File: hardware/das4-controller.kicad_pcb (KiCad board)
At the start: 2 copper layers, 51.1 x 94 mm, 16 parts, among them J1 USB-C (upstream, USB 2.0), J2 USB-A (hub port 1), J3 USB-A (hub port 2), J4 Key matrix 26p (TBD: pitch/ty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, SW1 Button, SW2 Button, SW3 Button, SW4 Button, SW5 Button

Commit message: Move volume encoder to its real position
The first photo trace located the top of the ~20 mm shaft, which
parallax shifted ~3 mm outward. Measured on the fit-check print against
the 50 mm scale bar, the body sits about flush with the bottom edge:
shaft centre (10.0, 5.8) instead of (10.6, 2.5).

Co-Authored-By: Claude Opus 5.5 <noreply@anthropic.com>
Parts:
- moved ENC1 3.35 mm to (112.5, 136.7)

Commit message: Use a no-switch encoder; knob has 20 detents and doesn't push
The original knob doesn't press, and a push-switch encoder can't fit:
with the body flush against the board edge its switch pins would land
off the board. Swap to the no-switch footprint, drop the encoder push
from the GPIO budget (36 pins) and record 20 detents per turn.

Co-Authored-By: Claude Opus 5.5 <noreply@anthropic.com>
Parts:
- ENC1: value Volume encoder (PEC12R-42xxF-S0024?) -> Volume encoder, no switch, 20 detents; footprint RotaryEncoder_Alps_EC12E-Switch_Vertical_H20mm -> RotaryEncoder_Alps_EC12E_Vertical_H20mm

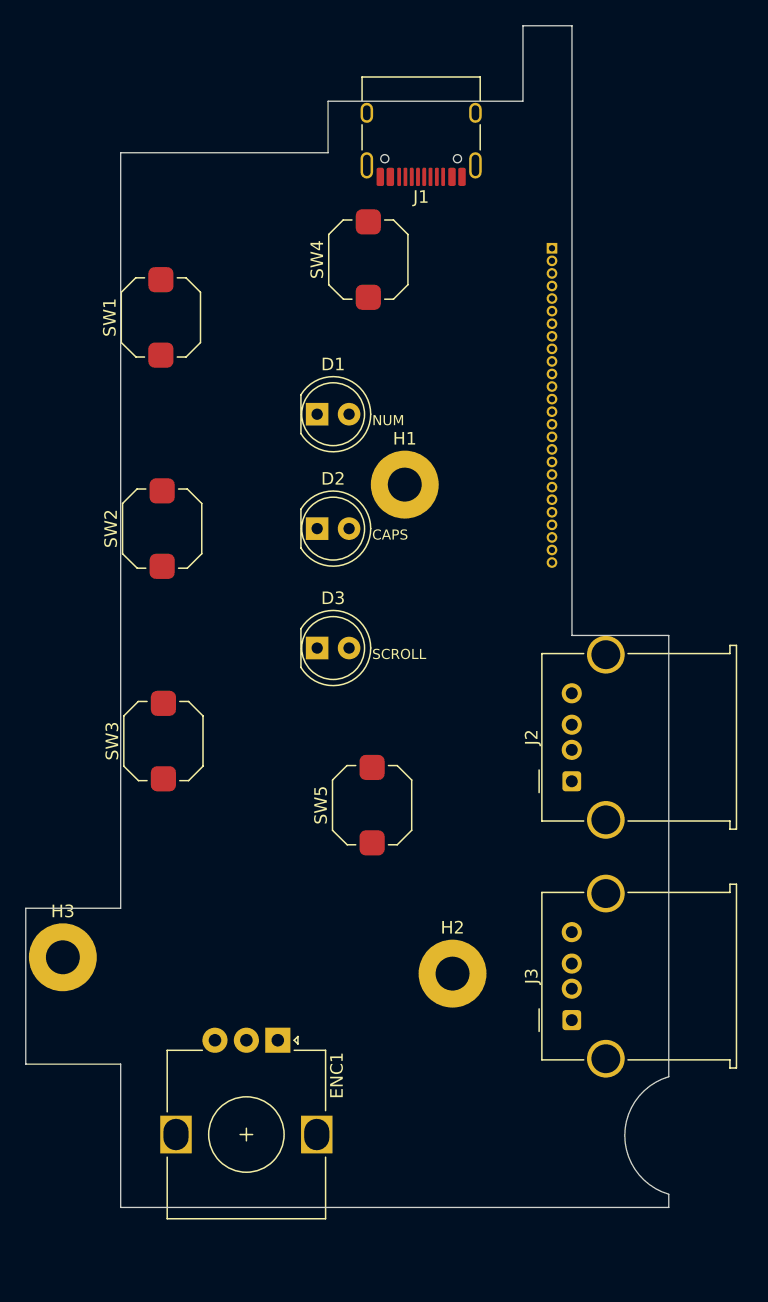
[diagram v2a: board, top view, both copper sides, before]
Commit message: Circuit in SKiDL, JLCPCB parts, and a placed 4-layer board
The circuit is now code (hardware/circuit/das4.py) and every part is a
real, in-stock JLCPCB part:
- RP2350B core copied from Raspberry Pi's minimal design (crystal, QSPI
  flash, 1.1 V regulator inductor, decoupling, BOOTSEL/RESET, SWD pads)
- CH334R USB 2.0 hub: USB-C upstream, two USB-A ports and the MCU
  downstream, powered from 3.3 V per the WCH datasheet; ESD on every
  port, polyfuses on the USB-A VBUS lines
- ME6211 3.3 V LDO, Alps EC12E no-switch encoder, 5 buttons, three
  5 V-driven lock LEDs, 26 key-matrix lines to GPIO21-46

The board is generated from the netlist: measured mechanical parts stay
put, everything else is placed in groups, on 4 layers with JLCPCB rules.
DRC is clean apart from routing, cosmetic silkscreen, and the CAPS LED
next to H1 (same as the original board).

Footprints, symbols and 3D models come from LCSC via easyeda2kicad, so
pads match what JLCPCB solders. docs/bom.md lists parts with live stock
(74 parts, ~$9 per board, 14 Extended types).

Co-Authored-By: Claude Opus 5.5 <noreply@anthropic.com>
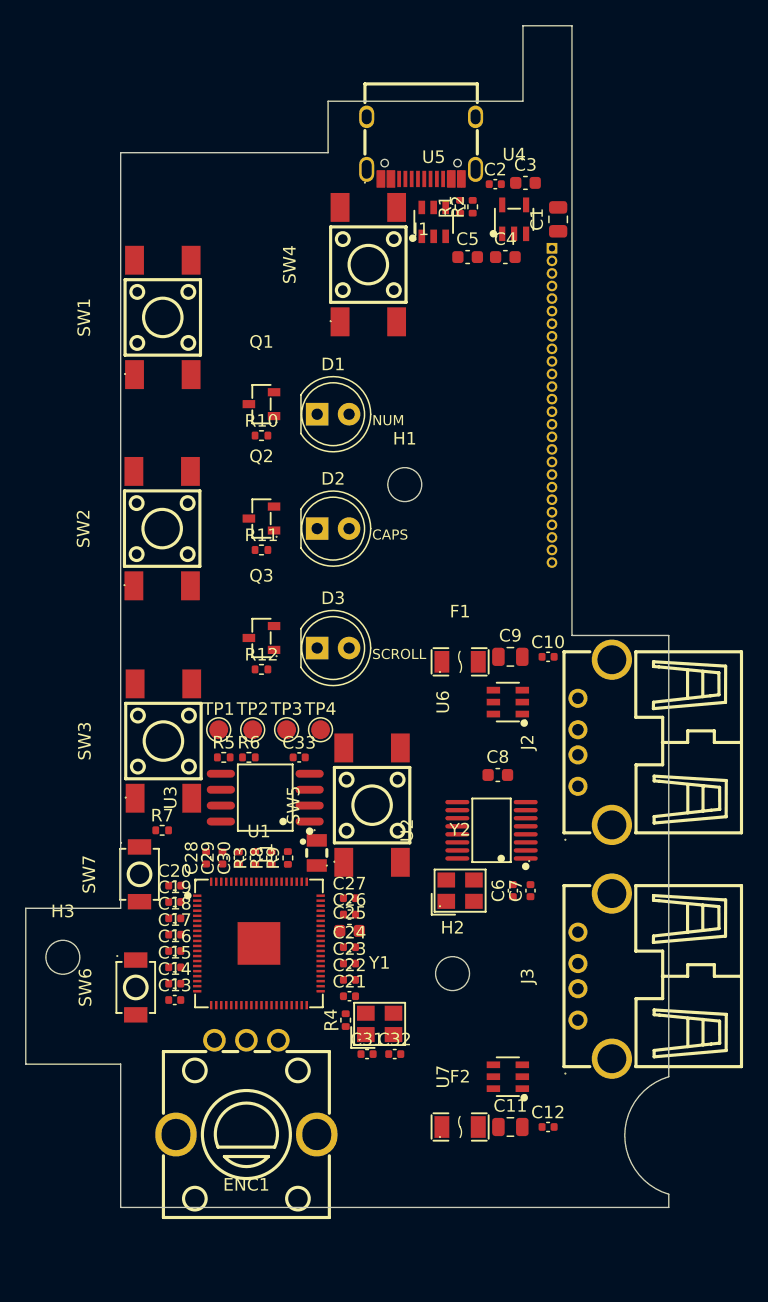
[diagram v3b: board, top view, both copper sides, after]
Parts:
- added C1: 22u, C_0805_2012Metric, F.Cu at (134.8, 71.4)
- added C10: 100n, C_0402_1005Metric, F.Cu at (134.0, 106.2)
- added C11: 22u, C_0805_2012Metric, F.Cu at (131.0, 143.6)
- added C12: 100n, C_0402_1005Metric, F.Cu at (134.0, 143.6)
- added C13: 100n, C_0402_1005Metric, F.Cu at (104.3, 133.5)
- added C14: 100n, C_0402_1005Metric, F.Cu at (104.3, 132.2)
- added C15: 100n, C_0402_1005Metric, F.Cu at (104.3, 130.9)
- added C16: 100n, C_0402_1005Metric, F.Cu at (104.3, 129.6)
- added C17: 100n, C_0402_1005Metric, F.Cu at (104.3, 128.3)
- added C18: 100n, C_0402_1005Metric, F.Cu at (104.3, 127.0)
- added C19: 100n, C_0402_1005Metric, F.Cu at (104.3, 125.7)
- added C2: 100n, C_0402_1005Metric, F.Cu at (129.8, 68.6)
- added C20: 100n, C_0402_1005Metric, F.Cu at (104.3, 124.4)
- added C21: 100n, C_0402_1005Metric, F.Cu at (118.2, 133.2)
- added C22: 100n, C_0402_1005Metric, F.Cu at (118.2, 131.9)
- added C23: 100n, C_0402_1005Metric, F.Cu at (118.2, 130.6)
- added C24: 4.7u, C_0402_1005Metric, F.Cu at (118.2, 129.3)
- added C25: 10u, C_0603_1608Metric, F.Cu at (118.2, 128.0)
- added C26: 4.7u, C_0402_1005Metric, F.Cu at (118.2, 126.7)
- added C27: 100n, C_0402_1005Metric, F.Cu at (118.2, 125.4)
- added C28: 100n, C_0402_1005Metric, F.Cu at (106.8, 122.2)
- added C29: 100n, C_0402_1005Metric, F.Cu at (108.1, 122.2)
- added C3: 10u, C_0603_1608Metric, F.Cu at (132.2, 68.5)
- added C30: 4.7u, C_0402_1005Metric, F.Cu at (109.4, 122.2)
- added C31: 15p, C_0402_1005Metric, F.Cu at (119.6, 137.8)
- added C32: 15p, C_0402_1005Metric, F.Cu at (121.8, 137.8)
- added C33: 100n, C_0402_1005Metric, F.Cu at (114.2, 114.2)
- added C4: 10u, C_0603_1608Metric, F.Cu at (130.6, 74.4)
- added C5: 10u, C_0603_1608Metric, F.Cu at (127.6, 74.4)
- added C6: 1u, C_0402_1005Metric, F.Cu at (131.2, 124.8)
- added C7: 100n, C_0402_1005Metric, F.Cu at (132.6, 124.8)
- added C8: 10u, C_0603_1608Metric, F.Cu at (130.0, 115.6)
- added C9: 22u, C_0805_2012Metric, F.Cu at (131.0, 106.2)
- added F1: 500mA, F1206, F.Cu at (127.0, 106.6)
- added F2: 500mA, F1206, F.Cu at (127.0, 143.6)
- added L1: 3.3uH, IND-SMD_L2.0-W1.6_AOTA-B201610S3R3-101-T, F.Cu at (115.6, 121.8)
- added Q1: 2N7002, SOT-23-3_L2.9-W1.3-P1.90-LS2.4-BR, F.Cu at (111.2, 86.1)
- added Q2: 2N7002, SOT-23-3_L2.9-W1.3-P1.90-LS2.4-BR, F.Cu at (111.2, 95.2)
- added Q3: 2N7002, SOT-23-3_L2.9-W1.3-P1.90-LS2.4-BR, F.Cu at (111.2, 104.7)
- added R1: 5.1k, R_0402_1005Metric, F.Cu at (127.0, 70.4)
- added R10: 330, R_0402_1005Metric, F.Cu at (111.2, 88.6)
- added R11: 330, R_0402_1005Metric, F.Cu at (111.2, 97.7)
- added R12: 330, R_0402_1005Metric, F.Cu at (111.2, 107.2)
- added R2: 5.1k, R_0402_1005Metric, F.Cu at (128.0, 70.4)
- added R3: 33, R_0402_1005Metric, F.Cu at (110.7, 122.2)
- added R4: 1k, R_0402_1005Metric, F.Cu at (117.9, 135.1)
- added R5: 10k, R_0402_1005Metric, F.Cu at (108.2, 114.2)
- added R6: 1k, R_0402_1005Metric, F.Cu at (110.2, 114.2)
- added R7: 1k, R_0402_1005Metric, F.Cu at (103.3, 120.0)
- added R8: 27, R_0402_1005Metric, F.Cu at (112.0, 122.2)
- added R9: 27, R_0402_1005Metric, F.Cu at (113.3, 122.2)
- added SW6: BOOTSEL, SW-SMD_L3.9-W3.0-P4.45, F.Cu at (101.2, 132.5)
- added SW7: RESET, SW-SMD_L3.9-W3.0-P4.45, F.Cu at (101.5, 123.5)
- added TP1: TestPoint, TestPoint_Pad_D1.5mm, F.Cu at (107.8, 112.0)
- added TP2: TestPoint, TestPoint_Pad_D1.5mm, F.Cu at (110.5, 112.0)
- added TP3: TestPoint, TestPoint_Pad_D1.5mm, F.Cu at (113.2, 112.0)
- added TP4: TestPoint, TestPoint_Pad_D1.5mm, F.Cu at (115.9, 112.0)
- added U1: RP2350B, QFN-80_L10.0-W10.0-P0.40-TL-EP3.4, F.Cu at (111.0, 129.0)
- added U2: CH334R, QSOP-16_L4.9-W3.9-P0.64-LS6.0-BL, F.Cu at (129.5, 120.0)
- added U3: W25Q128JVS, SOIC-8_L5.3-W5.3-P1.27-LS8.0-BL, F.Cu at (111.5, 117.4)
- added U4: ME6211C33M5G-N, SOT-23-5_L3.0-W1.7-P0.95-LS2.8-BL, F.Cu at (131.3, 71.4)
- added U5: USBLC6-2SC6, SOT-23-6_L2.9-W1.6-P0.95-LS2.8-BL, F.Cu at (124.9, 71.6)
- added U6: USBLC6-2SC6, SOT-23-6_L2.9-W1.6-P0.95-LS2.8-BL, F.Cu at (130.8, 109.8)
- added U7: USBLC6-2SC6, SOT-23-6_L2.9-W1.6-P0.95-LS2.8-BL, F.Cu at (130.8, 139.6)
- added Y1: 12MHz, CRYSTAL-SMD_4P-L3.2-W2.5-BL, F.Cu at (120.6, 135.4)
- added Y2: 12MHz, CRYSTAL-SMD_4P-L3.2-W2.5-BL, F.Cu at (127.0, 124.8)
- D1: value NUM -> NUM (white)
- D2: value CAPS -> CAPS (white)
- D3: value SCROLL -> SCROLL (white)
- ENC1: value Volume encoder, no switch, 20 detents -> EC12E24204A2; footprint RotaryEncoder_Alps_EC12E_Vertical_H20mm -> SW-TH_EC12E24204A2
- H1, H2, H3: value MountingHole_2.7mm_M2.5_Pad -> MountingHole_2.7mm_M2.5; footprint MountingHole_2.7mm_M2.5_Pad -> MountingHole_2.7mm_M2.5
- J1: value USB-C (upstream, USB 2.0) -> USB-C; footprint USB_C_Receptacle_HRO_TYPE-C-31-M-12 -> USB-C_SMD-TYPE-C-31-M-12_1
- J2: value USB-A (hub port 1) -> USB-A 1; footprint USB_A_Molex_67643_Horizontal -> USB-A-TH_AF-WJDG
- J3: value USB-A (hub port 2) -> USB-A 2; footprint USB_A_Molex_67643_Horizontal -> USB-A-TH_AF-WJDG
- J4: value Key matrix 26p (TBD: pitch/type) -> Key matrix
- SW1: value Button -> Button 1; footprint SW_Push_1TS009xxxx-xxxx-xxxx_6x6x5mm -> SW-SMD_4P-L6.0-W6.0-P4.50-LS9.0_H5.0
- SW2: value Button -> Button 2; footprint SW_Push_1TS009xxxx-xxxx-xxxx_6x6x5mm -> SW-SMD_4P-L6.0-W6.0-P4.50-LS9.0_H5.0
- SW3: value Button -> Button 3; footprint SW_Push_1TS009xxxx-xxxx-xxxx_6x6x5mm -> SW-SMD_4P-L6.0-W6.0-P4.50-LS9.0_H5.0
- SW4: value Button -> Button 4; footprint SW_Push_1TS009xxxx-xxxx-xxxx_6x6x5mm -> SW-SMD_4P-L6.0-W6.0-P4.50-LS9.0_H5.0
- SW5: value Button -> Button 5; footprint SW_Push_1TS009xxxx-xxxx-xxxx_6x6x5mm -> SW-SMD_4P-L6.0-W6.0-P4.50-LS9.0_H5.0
- moved ENC1 4.51 mm to (110.0, 140.4), turned to 180 degrees
- moved J3 3.95 mm to (137.7, 131.6)
- moved J2 3.60 mm to (137.7, 113.0)
- moved J1 1.74 mm to (123.9, 65.7)
- moved SW4 0.40 mm to (119.7, 75.0)
- moved SW1 0.15 mm to (103.3, 79.2)
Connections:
- D1 pad 1: (no net) -> LED_NUM_K
- D1 pad 2: (no net) -> LED_NUM_A
- D2 pad 1: (no net) -> LED_CAPS_K
- D2 pad 2: (no net) -> LED_CAPS_A
- D3 pad 1: (no net) -> LED_SCROLL_K
- D3 pad 2: (no net) -> LED_SCROLL_A
- ENC1 pad A: (no net) -> ENC_A
- ENC1 pad B: (no net) -> ENC_B
- ENC1 pad C: (no net) -> GND
- J1 pad A5: (no net) -> N$1
- J1 pad A6: (no net) -> USB_UP_D+
- J1 pad A7: (no net) -> USB_UP_D-
- J1 pad B5: (no net) -> N$2
- J1 pad B6: (no net) -> USB_UP_D+
- J1 pad B7: (no net) -> USB_UP_D-
- J2 pad 1: (no net) -> VBUS_A1
- J2 pad 2: (no net) -> USB_A1_D-
- J2 pad 3: (no net) -> USB_A1_D+
- J2 pad 4: (no net) -> GND
- J3 pad 1: (no net) -> VBUS_A2
- J3 pad 2: (no net) -> USB_A2_D-
- J3 pad 3: (no net) -> USB_A2_D+
- J3 pad 4: (no net) -> GND
- J4 pad 1: (no net) -> KM1
- J4 pad 10: (no net) -> KM10
- J4 pad 11: (no net) -> KM11
- J4 pad 12: (no net) -> KM12
- J4 pad 13: (no net) -> KM13
- J4 pad 14: (no net) -> KM14
- J4 pad 15: (no net) -> KM15
- J4 pad 16: (no net) -> KM16
- J4 pad 17: (no net) -> KM17
- J4 pad 18: (no net) -> KM18
- J4 pad 19: (no net) -> KM19
- J4 pad 2: (no net) -> KM2
- J4 pad 20: (no net) -> KM20
- J4 pad 21: (no net) -> KM21
- J4 pad 22: (no net) -> KM22
- J4 pad 23: (no net) -> KM23
- J4 pad 24: (no net) -> KM24
- J4 pad 25: (no net) -> KM25
- J4 pad 26: (no net) -> KM26
- J4 pad 3: (no net) -> KM3
- J4 pad 4: (no net) -> KM4
- J4 pad 5: (no net) -> KM5
- J4 pad 6: (no net) -> KM6
- J4 pad 7: (no net) -> KM7
- J4 pad 8: (no net) -> KM8
- J4 pad 9: (no net) -> KM9
- SW1 pad 1: (no net) -> BTN1
- SW1 pad 2: (no net) -> BTN1
- SW2 pad 1: (no net) -> BTN2
- SW2 pad 2: (no net) -> BTN2
- SW3 pad 1: (no net) -> BTN3
- SW3 pad 2: (no net) -> BTN3
- SW4 pad 1: (no net) -> BTN4
- SW4 pad 2: (no net) -> BTN4
- SW5 pad 1: (no net) -> BTN5
- SW5 pad 2: (no net) -> BTN5
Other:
- copper layers 2 -> 4
- board text added: "DRAFT - not routed yet. Outline from measurements + photos,"
- board text added: "see docs/measurements.md."
- board text removed: "DRAFT - outline traced from a photo, scaled to the 83.9 mm body."
- board text removed: "Verify with calipers before ordering. See docs/measurements.md."

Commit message: Make the lock LEDs RGB (WS2812D-F5)
Swap the three white LEDs and their 2N7002/330R drivers for WS2812D-F5
addressable RGB LEDs in the same 5 mm through-hole shape, so the colour
is set in firmware. One GPIO (GPIO11) drives the chain NUM -> CAPS ->
SCROLL through a 74AHCT1G125 level shifter (the LEDs want a 5 V data
signal) and a 33R series resistor; 100 nF per LED. Frees GPIO12/13.

Co-Authored-By: Claude Opus 5.5 <noreply@anthropic.com>
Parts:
- removed Q1, Q2, Q3: 2N7002, SOT-23-3_L2.9-W1.3-P1.90-LS2.4-BR
- removed R11, R12: 330, R_0402_1005Metric
- added C34: 100n, C_0402_1005Metric, F.Cu at (113.4, 89.6)
- added C35: 100n, C_0402_1005Metric, F.Cu at (111.2, 85.6)
- added C36: 100n, C_0402_1005Metric, F.Cu at (111.2, 94.7)
- added C37: 100n, C_0402_1005Metric, F.Cu at (111.2, 104.2)
- added U8: 74AHCT1G125GV, SOT-23-5_L3.0-W1.7-P0.95-LS2.8-BL, F.Cu at (111.2, 89.6)
- D1: value NUM (white) -> NUM (RGB); footprint LED_D5.0mm -> LED-TH_4P-BD5.8-P1.27_WS2812D-F5-12MA-C1
- D2: value CAPS (white) -> CAPS (RGB); footprint LED_D5.0mm -> LED-TH_4P-BD5.8-P1.27_WS2812D-F5-12MA-C1
- D3: value SCROLL (white) -> SCROLL (RGB); footprint LED_D5.0mm -> LED-TH_4P-BD5.8-P1.27_WS2812D-F5-12MA-C1
- R10: value 330 -> 33
- moved R10 3.40 mm to (111.2, 92.0)
- moved D1 1.27 mm to (116.9, 86.9)
- moved D2 1.27 mm to (116.9, 96.0)
- moved D3 1.27 mm to (116.9, 105.5)
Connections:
- D1 pad 1: LED_NUM_K -> LED_DIN2
- D1 pad 2: LED_NUM_A -> +5V
- D2 pad 1: LED_CAPS_K -> LED_DIN3
- D2 pad 2: LED_CAPS_A -> +5V
- D3 pad 1: LED_SCROLL_K -> (no net)
- D3 pad 2: LED_SCROLL_A -> +5V
- R10 pad 1: +5V -> N$10
- R10 pad 2: LED_NUM_A -> LED_DIN1
- U1 pad 11: LED_CAPS -> (no net)
- U1 pad 12: LED_SCROLL -> (no net)
- U1 pad 9: LED_NUM -> LED_DATA_3V3

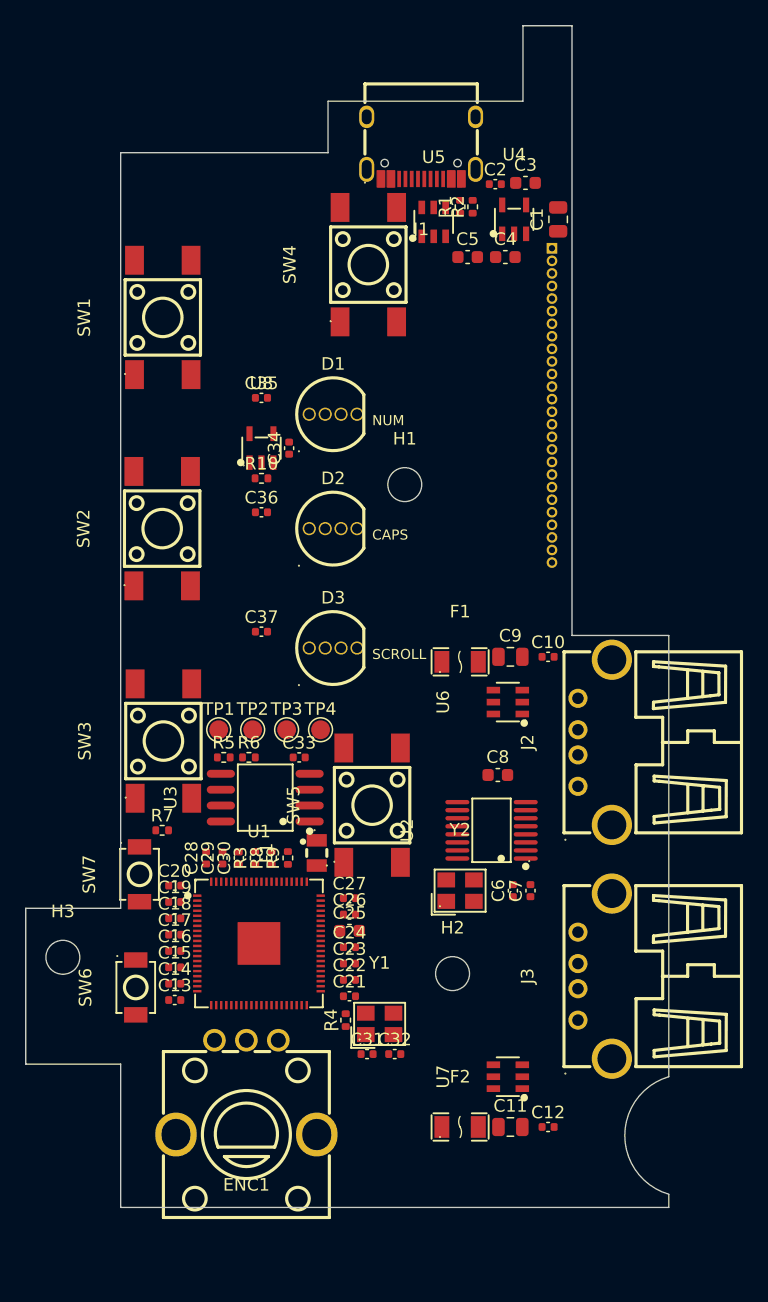
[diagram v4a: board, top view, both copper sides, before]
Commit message: Cut JLCPCB Extended parts from 15 to 5; add order-file export
Swap to JLCPCB Basic parts where it's safe and move the easy parts to
hand soldering, so only the RP2350B, CH334R, USB-C, inductor and crystal
carry Extended fees:
- AMS1117-3.3 instead of ME6211; 22R instead of 27R USB resistors
- drop the USBLC6 ESD chips (the CH334R has 6 kV ESD on its USB pins)
  and the USB-A polyfuses (the PC's port limits current)
- drive the WS2812 chain with the first LED powered through a 1N4148W,
  instead of a 74AHCT level shifter
- Basic TS-1187A BOOTSEL/RESET buttons
- USB-A, encoder, LEDs and the 6x6 buttons are marked Assembly=hand:
  out of the JLCPCB BOM/CPL, listed separately in docs/bom.md

`make fab` writes the Gerber zip, bom.csv and cpl.csv for JLCPCB; the
zip is named quote-only until the board is routed.

Co-Authored-By: Claude Opus 5.5 <noreply@anthropic.com>
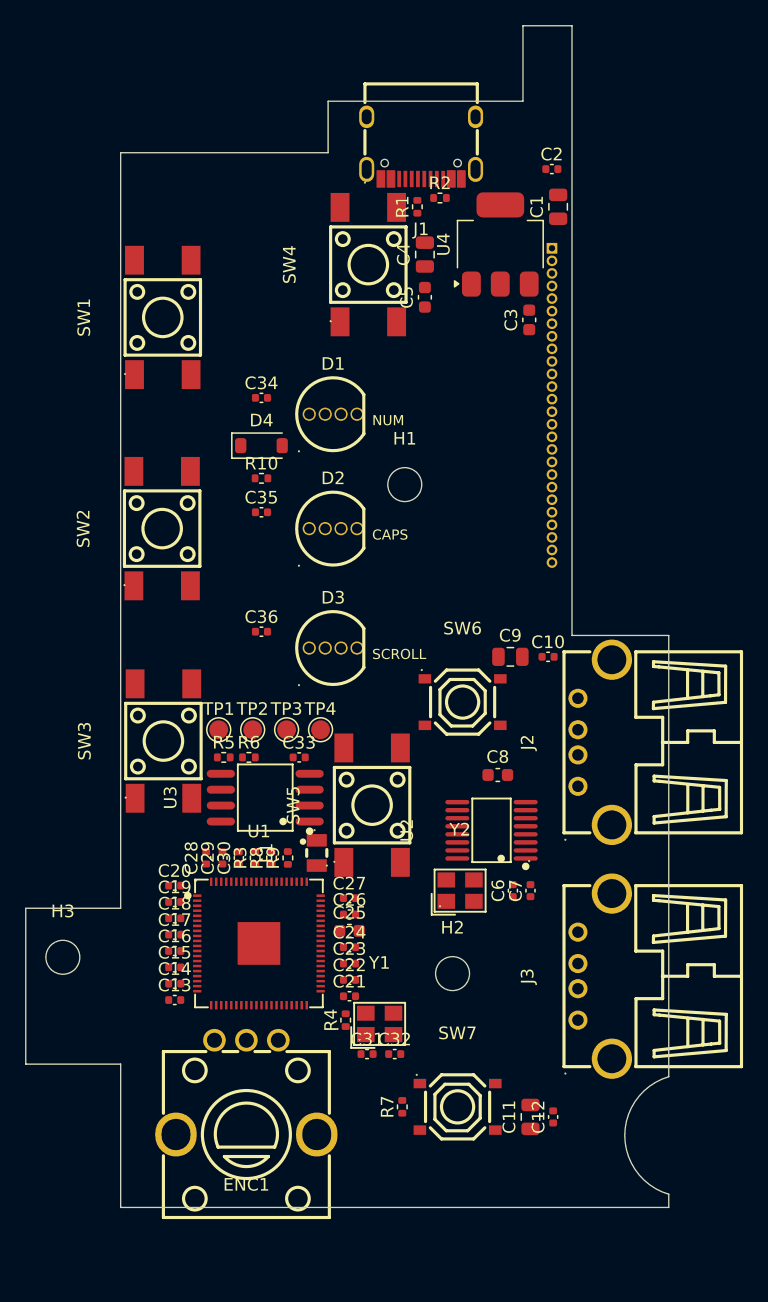
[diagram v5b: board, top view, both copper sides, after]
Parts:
- removed C37: 100n, C_0402_1005Metric
- removed F1, F2: 500mA, F1206
- removed U5, U6, U7: USBLC6-2SC6, SOT-23-6_L2.9-W1.6-P0.95-LS2.8-BL
- removed U8: 74AHCT1G125GV, SOT-23-5_L3.0-W1.7-P0.95-LS2.8-BL
- added D4: 1N4148W, D_SOD-123, F.Cu at (111.2, 89.4)
- C4: value 10u -> 22u; footprint C_0603_1608Metric -> C_0805_2012Metric
- R8, R9: value 27 -> 22
- SW6, SW7: footprint SW-SMD_L3.9-W3.0-P4.45 -> SW-SMD_4P-L5.1-W5.1-P3.70-LS6.5-TL_H1.5
- U4: value ME6211C33M5G-N -> AMS1117-3.3; footprint SOT-23-5_L3.0-W1.7-P0.95-LS2.8-BL -> SOT-223-3_TabPin2
- moved SW6 34.5 mm to (127.2, 109.8), turned to 0 degrees
- moved SW7 31.3 mm to (126.8, 142.0), turned to 0 degrees
- moved R7 29.1 mm to (122.4, 142.0), turned to 90 degrees
- moved C3 10.9 mm to (132.5, 79.4), turned to 90 degrees
- moved C36 9.50 mm to (111.2, 104.2)
- moved C35 9.10 mm to (111.2, 94.7)
- moved C4 6.40 mm to (124.2, 74.2), turned to 90 degrees
- moved C5 4.67 mm to (124.2, 77.6), turned to 90 degrees
- moved C2 4.66 mm to (134.3, 67.4)
- moved C34 4.57 mm to (111.2, 85.6), turned to 0 degrees
- moved R1 3.40 mm to (123.6, 70.4)
- moved R2 2.69 mm to (125.4, 69.7), turned to 0 degrees
- moved U4 2.28 mm to (130.2, 73.4), turned to 90 degrees
- moved C11 1.79 mm to (132.6, 142.8), turned to 90 degrees
- moved C1 1.00 mm to (134.8, 70.4)
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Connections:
- C10 pad 1: VBUS_A1 -> +5V
- C11 pad 1: VBUS_A2 -> +5V
- C12 pad 1: VBUS_A2 -> +5V
- C34 pad 1: +5V -> LED1_VDD
- C9 pad 1: VBUS_A1 -> +5V
- D1 pad 2: +5V -> LED1_VDD
- J2 pad 1: VBUS_A1 -> +5V
- J3 pad 1: VBUS_A2 -> +5V
- SW6 pad 2: GND -> USB_BOOT
- SW7 pad 2: RUN_BTN -> RUN
- U1 pad 9: LED_DATA_3V3 -> N$10
- U4 pad 1: +5V -> GND
- U4 pad 2: GND -> +3V3
